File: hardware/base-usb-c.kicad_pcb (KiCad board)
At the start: 4 copper layers, 100 x 85 mm, 158 parts, among them J101 USB-A, J102 USB-C, J103 TNG-Power-TOP, J105 TNG-Data-TOP, P101 Debug, P102 PE, P202 PWR IN, SW101 BOOT, T201 744272251, U101 USB2517, U102 MIC2026-1YM, U103 82400152, U104 STM32F070CBT6, U105 TPD4S010DQA, U106 TPD4S010DQA, U107 TPD4S010DQA, U108 82400152, U110 TPS22975, U112 VN7140AS, U201 AZ1117EH, U203 BD90640HFP, U204 PAC1933, X101 24MHz, X102 8MHz

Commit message: fix values
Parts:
- C128: value 1µF -> 1uF
- C203, C216, C219, C220: value 100µF -> 100uF
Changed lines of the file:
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@@
       (effects (font (size 0.59944 0.59944) (thickness 0.12446)))
     )
-    (fp_text value 100µF (at 0.95 -0.375 90) (layer F.Fab)
+    (fp_text value 100uF (at 0.95 -0.375 90) (layer F.Fab)
       (effects (font (size 0.59944 0.59944) (thickness 0.12446)))
     )
@@
       (effects (font (size 0.59944 0.59944) (thickness 0.12446)))
     )
-    (fp_text value 100µF (at 0.95 -0.375 90) (layer F.Fab)
+    (fp_text value 100uF (at 0.95 -0.375 90) (layer F.Fab)
       (effects (font (size 0.59944 0.59944) (thickness 0.12446)))
     )
@@
       (effects (font (size 0.2 0.2) (thickness 0.05)))
     )
-    (fp_text value 1µF (at 0 -0.15) (layer F.Fab)
+    (fp_text value 1uF (at 0 -0.15) (layer F.Fab)
       (effects (font (size 0.2 0.2) (thickness 0.05)))
     )
@@
       (effects (font (size 0.59944 0.59944) (thickness 0.12446)))
     )
-    (fp_text value 100µF (at 0.95 -0.375) (layer F.Fab)
+    (fp_text value 100uF (at 0.95 -0.375) (layer F.Fab)
       (effects (font (size 0.59944 0.59944) (thickness 0.12446)))
     )
@@
       (effects (font (size 0.59944 0.59944) (thickness 0.12446)))
     )
-    (fp_text value 100µF (at 0.95 -0.375) (layer F.Fab)
+    (fp_text value 100uF (at 0.95 -0.375) (layer F.Fab)
       (effects (font (size 0.59944 0.59944) (thickness 0.12446)))
     )

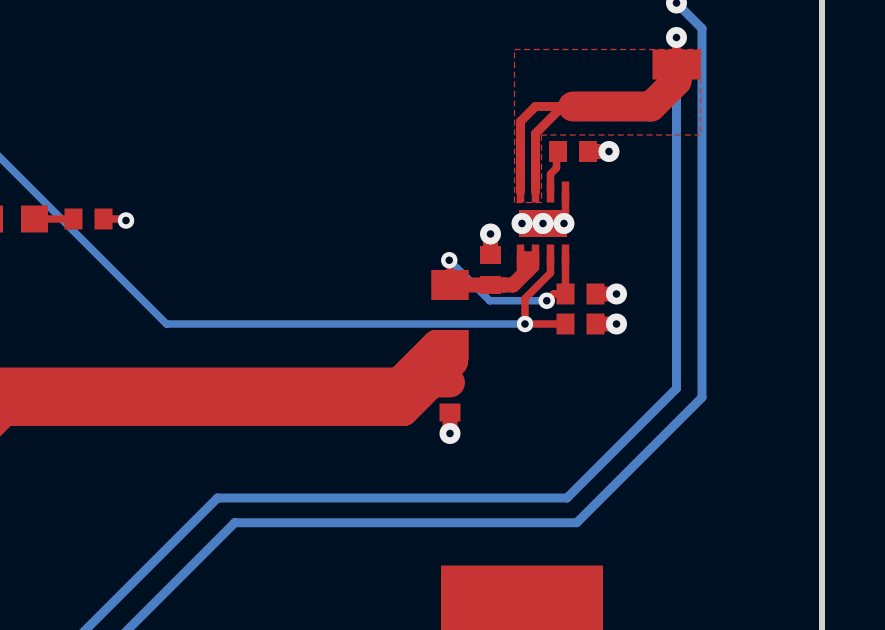
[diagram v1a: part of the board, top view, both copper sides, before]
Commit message: fix footprint
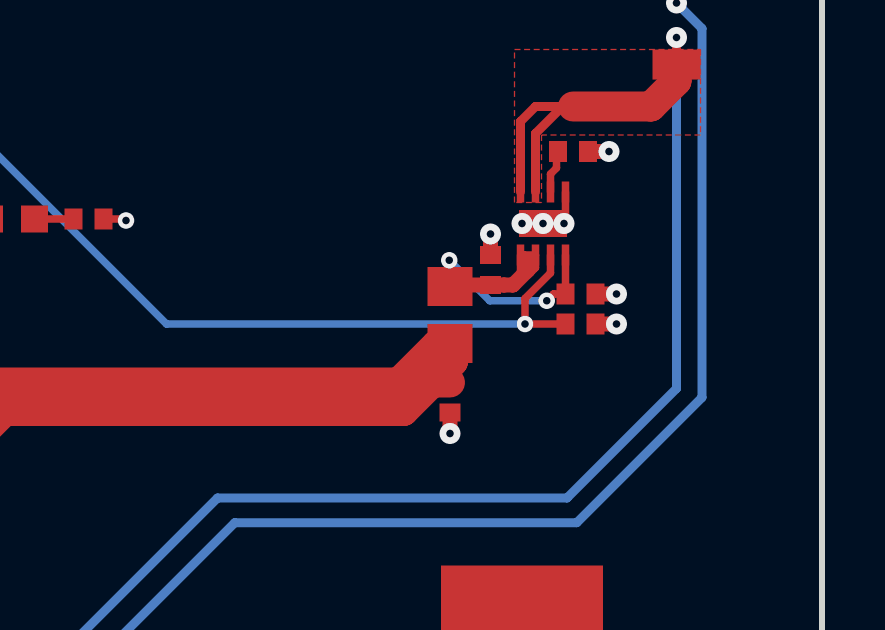
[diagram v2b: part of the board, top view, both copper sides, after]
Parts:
- L109: footprint kicad-libraries:R0805 -> kicad-libraries:R0805E

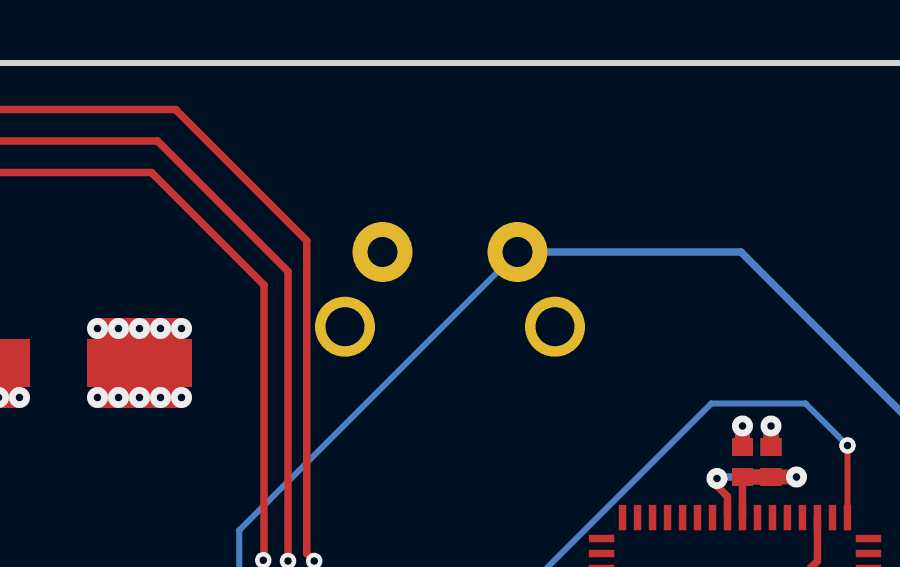
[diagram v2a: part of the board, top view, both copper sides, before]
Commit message: all footprints updated
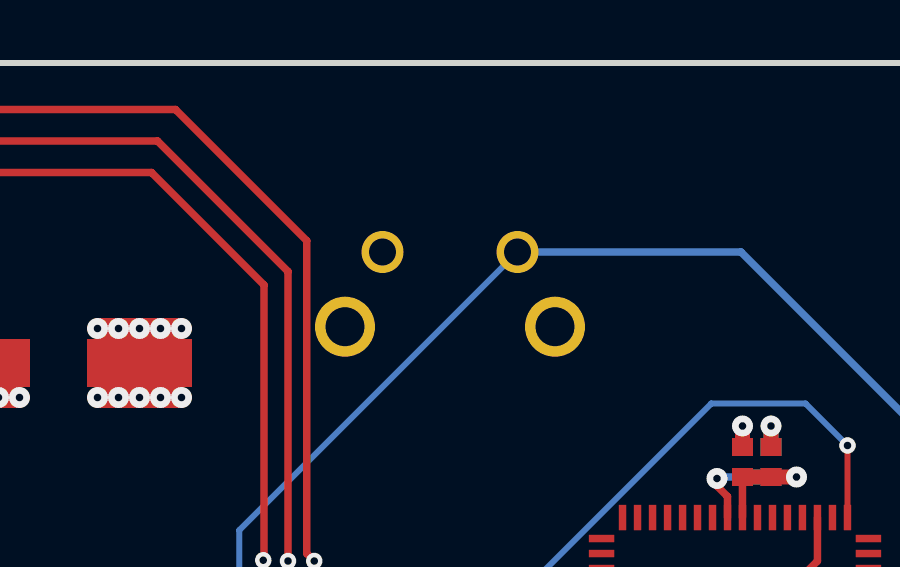
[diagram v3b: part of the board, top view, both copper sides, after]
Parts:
- C101, C102, C103, C104, C105, C106, C107, C110, C111, C112, C113, C114, C115, C116, C118, C119, C121, C122, C123, C124, C125, C126, C127, C128, C129, C130, C131, C132, C133, C134, C137, C138, C209, C214, C221, C222, C226: footprint C0402F -> kicad-libraries:C0402F
- C108, C109, C117, C141: footprint ELKO_63 -> kicad-libraries:ELKO_63
- C120, C140, C210, C217: footprint C0603F -> kicad-libraries:C0603F
- C135, C136, C201, C202, C204, C206, C207, C211, C215, C218, C223, C224, C225, C227: footprint C1206 -> kicad-libraries:C1206
- D101: footprint LED-LP -> kicad-libraries:LED-LP
- D102: footprint D0603F -> kicad-libraries:D0603F
- D202, D205, D206: footprint SOD-128 -> kicad-libraries:SOD-128
- J103, J105: footprint TNG-40-TOP -> kicad-libraries:TNG-40-TOP
- L101, L108, L201, R208, R212, R214, R215: footprint R0603F -> kicad-libraries:R0603F
- L102, L103, L104, L105, L106, L107, L110: footprint WE-CNSW-0603 -> kicad-libraries:WE-CNSW-0603
- L111, L203: footprint SRP7030 -> kicad-libraries:SRP7030
- L202: footprint WE-LHMI -> kicad-libraries:WE-LHMI
- LED101: footprint LED-RGB-LP -> kicad-libraries:LED-RGB-LP
- P202: footprint OQ_4P -> kicad-libraries:OQ_4P
- R101, R102, R103, R104, R105, R106, R107, R108, R109, R110, R111, R112, R113, R114, R115, R116, R117, R119, R120, R121, R122, R123, R218: footprint R0402F -> kicad-libraries:R0402F
- R204, R206, R207, R209, R219, R220, R221: footprint R1206 -> kicad-libraries:R1206
- T201: footprint WE-SL5 -> kicad-libraries:WE-SL5
- U103, U108: footprint SOT563-SPEC -> kicad-libraries:SOT563-SPEC
- U105, U106, U107: footprint TPD4S010DQA -> kicad-libraries:TPD4S010DQA
- U110: footprint WSON8-2x2 -> kicad-libraries:WSON8-2x2
- U203: footprint BD906XX-C-HRP7 -> kicad-libraries:BD906XX-C-HRP7
- X101: footprint CRYSTAL_3225 -> kicad-libraries:CRYSTAL_3225
